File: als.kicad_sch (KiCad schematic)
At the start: 2 parts, among them J11 Conn_02x12_Odd_Even, U14 TCA9802

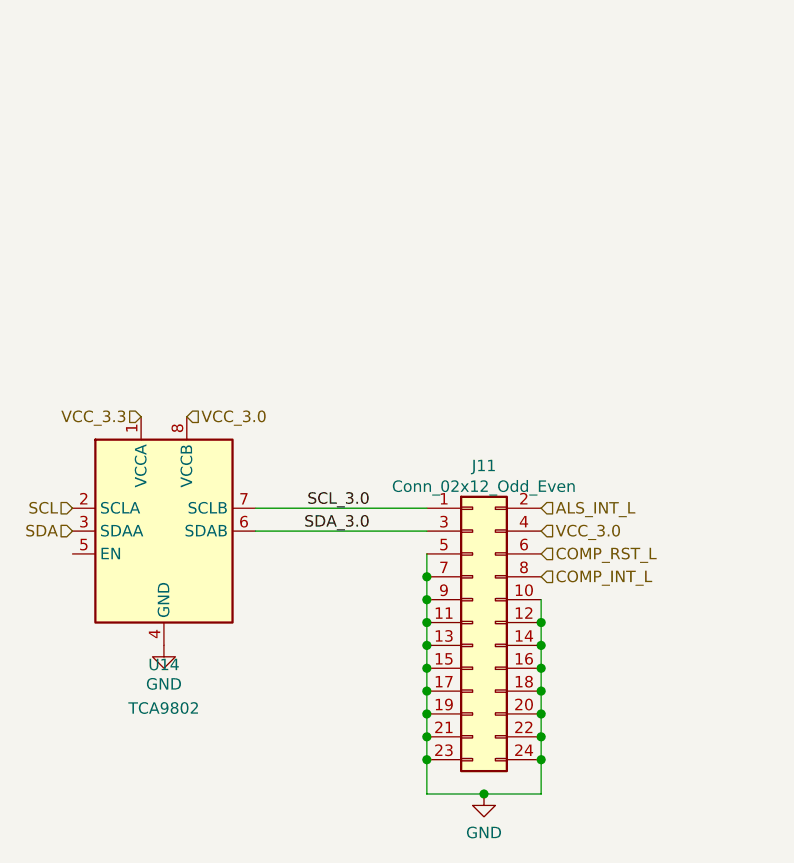
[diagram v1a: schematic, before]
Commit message: Fix (or ignore) all ERC and DRC errors.
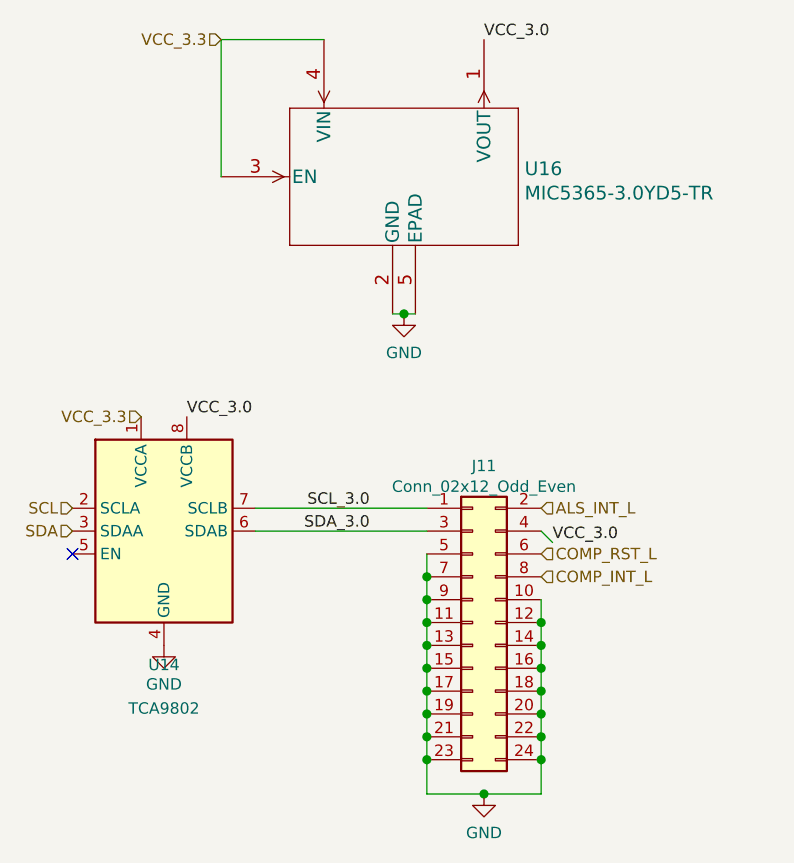
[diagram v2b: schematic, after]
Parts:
- added U16: MIC5365-3.0YD5-TR, Package_TO_SOT_SMD:SOT-23-5_HandSoldering, symbol MIC5365-3.0YD5-TR:MIC5365-3.0YD5-TR
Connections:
- net GND: now also U16.2 (GND), U16.5 (EPAD)
- net VCC_3.0: now also U16.1 (VOUT)
- net VCC_3.3: now also U16.3 (EN), U16.4 (VIN)
- no-connect marks 0 -> 1
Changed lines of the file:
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@@
 (kicad_sch (version 20210126) (generator eeschema)
   (paper "A4")
+  (junction (at 125.73 58.42) (diameter 1.016) (color 0 0 0 0))
   (junction (at 128.27 87.63) (diameter 1.016) (color 0 0 0 0))
   (junction (at 128.27 90.17) (diameter 1.016) (color 0 0 0 0))
@@
   (junction (at 140.97 105.41) (diameter 1.016) (color 0 0 0 0))
   (junction (at 140.97 107.95) (diameter 1.016) (color 0 0 0 0))
+  (no_connect (at 88.9 85.09))
+  (wire (pts (xy 105.41 27.94) (xy 105.41 43.18))
+    (stroke (width 0) (type solid) (color 0 0 0 0))
+  )
   (wire (pts (xy 109.22 80.01) (xy 128.27 80.01))
     (stroke (width 0) (type solid) (color 0 0 0 0))
@@
     (stroke (width 0) (type solid) (color 0 0 0 0))
   )
+  (wire (pts (xy 116.84 27.94) (xy 105.41 27.94))
+    (stroke (width 0) (type solid) (color 0 0 0 0))
+  )
+  (wire (pts (xy 124.46 58.42) (xy 125.73 58.42))
+    (stroke (width 0) (type solid) (color 0 0 0 0))
+  )
+  (wire (pts (xy 125.73 58.42) (xy 127 58.42))
+    (stroke (width 0) (type solid) (color 0 0 0 0))
+  )
   (wire (pts (xy 128.27 85.09) (xy 128.27 87.63))
     (stroke (width 0) (type solid) (color 0 0 0 0))
@@
   (wire (pts (xy 140.97 111.76) (xy 134.62 111.76))
     (stroke (width 0) (type solid) (color 0 0 0 0))
+  )
+  (wire (pts (xy 142.24 83.82) (xy 140.97 82.55))
+    (stroke (width 0) (type solid) (color 0 0 0 0))
+  )
+  (label "VCC_3.0" (at 101.6 69.85 0)
+    (effects (font (size 1.27 1.27)) (justify left bottom))
   )
   (label "SCL_3.0" (at 121.92 80.01 180)
@@
     (effects (font (size 1.27 1.27)) (justify right bottom))
   )
+  (label "VCC_3.0" (at 134.62 27.94 0)
+    (effects (font (size 1.27 1.27)) (justify left bottom))
+  )
+  (label "VCC_3.0" (at 142.24 83.82 0)
+    (effects (font (size 1.27 1.27)) (justify left bottom))
+  )
   (hierarchical_label "SCL" (shape input) (at 88.9 80.01 180)
     (effects (font (size 1.27 1.27)) (justify right))
@@
     (effects (font (size 1.27 1.27)) (justify right))
   )
-  (hierarchical_label "VCC_3.0" (shape input) (at 101.6 69.85 0)
-    (effects (font (size 1.27 1.27)) (justify left))
+  (hierarchical_label "VCC_3.3" (shape input) (at 105.41 27.94 180)
+    (effects (font (size 1.27 1.27)) (justify right))
   )
   (hierarchical_label "ALS_INT_L" (shape input) (at 140.97 80.01 0)
     (effects (font (size 1.27 1.27)) (justify left))
   )
-  (hierarchical_label "VCC_3.0" (shape input) (at 140.97 82.55 0)
-    (effects (font (size 1.27 1.27)) (justify left))
-  )
   (hierarchical_label "COMP_RST_L" (shape input) (at 140.97 85.09 0)
     (effects (font (size 1.27 1.27)) (justify left))
@@
     )
     (property "Datasheet" "" (id 3) (at 99.06 95.25 0)
+      (effects (font (size 1.27 1.27)) hide)
+    )
+    (pin "1")
+  )
+  (symbol (lib_id "power:GND") (at 125.73 58.42 0) (unit 1)
+    (in_bom yes) (on_board yes) (fields_autoplaced)
+    (property "Reference" "#PWR0139" (id 0) (at 125.73 64.77 0)
+      (effects (font (size 1.27 1.27)) hide)
+    )
+    (property "Value" "GND" (id 1) (at 125.73 62.7444 0))
+    (property "Footprint" "" (id 2) (at 125.73 58.42 0)
+      (effects (font (size 1.27 1.27)) hide)
+    )
+    (property "Datasheet" "" (id 3) (at 125.73 58.42 0)
       (effects (font (size 1.27 1.27)) hide)
     )
@@
     (pin "8")
   )
+  (symbol (lib_id "MIC5365-3.0YD5-TR:MIC5365-3.0YD5-TR") (at 105.41 40.64 0) (unit 1)
+    (in_bom yes) (on_board yes) (fields_autoplaced)
+    (property "Reference" "U16" (id 0) (at 139.1285 42.2924 0)
+      (effects (font (size 1.524 1.524)) (justify left))
+    )
+    (property "Value" "MIC5365-3.0YD5-TR" (id 1) (at 139.1285 45 0)
+      (effects (font (size 1.524 1.524)) (justify left))
+    )
+    (property "Footprint" "Package_TO_SOT_SMD:SOT-23-5_HandSoldering" (id 2) (at 124.46 44.45 0)
+      (effects (font (size 1.524 1.524)) hide)
+    )
+    (property "Datasheet" "" (id 3) (at 105.41 40.64 0)
+      (effects (font (size 1.524 1.524)))
+    )
+    (pin "1")
+    (pin "2")
+    (pin "3")
+    (pin "4")
+    (pin "5")
+  )
 )
